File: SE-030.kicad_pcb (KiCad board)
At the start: 4 copper layers, 109.1 x 99.6 mm, 78 parts, among them J1 MacSEPDS, J2 JTAG, SW1 OSCSEL, U1 XC95144XL-TQ100, U10 39SF040, U11 39SF040, U13 74AHCT573, U14 MC68HC000FN20, U15 74AHCT573, U16 74AHCT573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

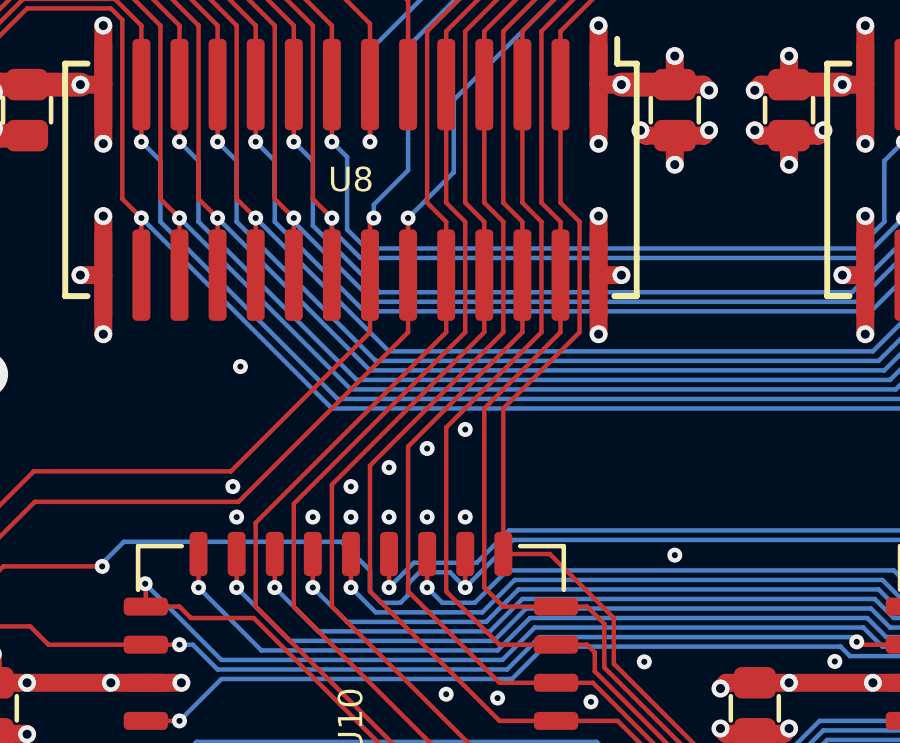
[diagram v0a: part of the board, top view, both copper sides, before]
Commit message: Update SE-030.kicad_pcb
More via stitching
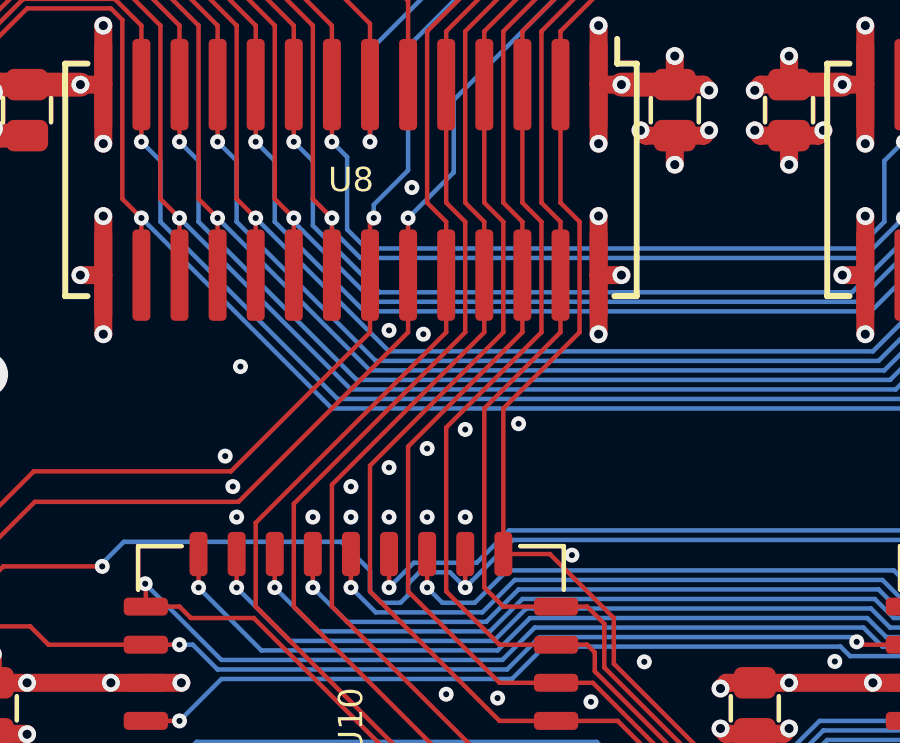
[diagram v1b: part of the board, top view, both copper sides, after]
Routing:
- net GND: vias 428 -> 433

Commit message: Documentation update
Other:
- board text added: "4410A"
- board text removed: "4406A"
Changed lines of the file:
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@@
     (solder_paste_margin -0.025)
     (attr smd)
-    (fp_text reference U14 (at 0 0) (layer F.SilkS)
+    (fp_text reference U14 (at 0 -1.27) (layer F.SilkS)
       (effects (font (size 0.8128 0.8128) (thickness 0.2032)))
     )
@@
     (fp_line (start -12.37 -10.71) (end -12.9 -10.71) (layer F.CrtYd) (width 0.05))
     (fp_line (start -12.9 -10.71) (end -12.9 0) (layer F.CrtYd) (width 0.05))
-    (fp_text user %R (at 0 0) (layer F.Fab)
+    (fp_text user %R (at 0 -1.27) (layer F.Fab)
       (effects (font (size 0.8128 0.8128) (thickness 0.2032)))
     )
@@
     )
   )
-  (gr_text Warp-SE (at 181.356 43.18) (layer F.SilkS)
+  (gr_text Warp-SE (at 181.356 43.815) (layer F.SilkS)
     (effects (font (size 1.524 1.524) (thickness 0.3)))
   )
-  (gr_text "Accelerator for Mac SE" (at 181.356 45.466) (layer F.SilkS)
+  (gr_text "Accelerator for Mac SE" (at 181.356 46.101) (layer F.SilkS)
     (effects (font (size 1.016 1.016) (thickness 0.2032)))
   )
-  (gr_text GW (at 159.258 45.6565) (layer F.SilkS)
+  (gr_text GW (at 159.258 46.2915) (layer F.SilkS)
     (effects (font (size 1.5 1.5) (thickness 0.3)) (justify right))
   )
-  (gr_text 4406A (at 159.258 45.72) (layer F.SilkS)
+  (gr_text 4410A (at 159.258 46.355) (layer F.SilkS)
     (effects (font (size 1.5 1.5) (thickness 0.3)) (justify left))
   )
-  (gr_text "Garrett’s Workshop" (at 161.163 42.926) (layer F.SilkS)
+  (gr_text "Garrett’s Workshop" (at 161.163 43.561) (layer F.SilkS)
     (effects (font (size 1.524 1.524) (thickness 0.225)))
   )
@@
   (segment (start 109.6 108.1) (end 108.9 108.1) (width 0.5) (layer F.Cu) (net 1))
   (via (at 198.882 94.0435) (size 0.5) (drill 0.2) (layers F.Cu B.Cu) (net 1))
-  (via (at 154.94 98.933) (size 0.5) (drill 0.2) (layers F.Cu B.Cu) (net 1))
-  (via (at 156.21 98.933) (size 0.5) (drill 0.2) (layers F.Cu B.Cu) (net 1))
-  (via (at 151.13 98.933) (size 0.5) (drill 0.2) (layers F.Cu B.Cu) (net 1))
-  (via (at 149.86 98.933) (size 0.5) (drill 0.2) (layers F.Cu B.Cu) (net 1))
-  (via (at 148.59 98.933) (size 0.5) (drill 0.2) (layers F.Cu B.Cu) (net 1))
-  (via (at 144.78 98.933) (size 0.5) (drill 0.2) (layers F.Cu B.Cu) (net 1))
-  (via (at 143.51 98.933) (size 0.5) (drill 0.2) (layers F.Cu B.Cu) (net 1))
+  (via (at 154.94 102.6795) (size 0.5) (drill 0.2) (layers F.Cu B.Cu) (net 1))
+  (via (at 156.21 101.4095) (size 0.5) (drill 0.2) (layers F.Cu B.Cu) (net 1))
+  (via (at 151.257 103.759) (size 0.5) (drill 0.2) (layers F.Cu B.Cu) (net 1))
+  (via (at 149.987 103.6955) (size 0.5) (drill 0.2) (layers F.Cu B.Cu) (net 1))
+  (via (at 148.717 102.9335) (size 0.5) (drill 0.2) (layers F.Cu B.Cu) (net 1))
+  (via (at 144.907 102.8065) (size 0.5) (drill 0.2) (layers F.Cu B.Cu) (net 1))
+  (via (at 143.637 102.8065) (size 0.5) (drill 0.2) (layers F.Cu B.Cu) (net 1))
   (via (at 154.94 93.98) (size 0.5) (drill 0.2) (layers F.Cu B.Cu) (net 1))
   (via (at 144.78 93.98) (size 0.5) (drill 0.2) (layers F.Cu B.Cu) (net 1))
@@
   (via (at 114.15 78.35) (size 1) (drill 0.5) (layers F.Cu B.Cu) (net 1))
   (via (at 120.45 96.35) (size 0.5) (drill 0.2) (layers F.Cu B.Cu) (net 1))
-  (via (at 153.67 98.933) (size 0.5) (drill 0.2) (layers F.Cu B.Cu) (net 1))
+  (via (at 153.797 103.759) (size 0.5) (drill 0.2) (layers F.Cu B.Cu) (net 1))
   (via (at 173.228 56.515) (size 0.6) (drill 0.3) (layers F.Cu B.Cu) (net 1))
   (segment (start 173.052 56.691) (end 173.228 56.515) (width 0.6) (layer F.Cu) (net 1))
@@
   (via (at 149.225 81.407) (size 0.5) (drill 0.2) (layers F.Cu B.Cu) (net 1))
   (via (at 147.32 93.98) (size 0.5) (drill 0.2) (layers F.Cu B.Cu) (net 1))
-  (via (at 146.05 98.933) (size 0.5) (drill 0.2) (layers F.Cu B.Cu) (net 1))
-  (via (at 142.24 98.933) (size 0.5) (drill 0.2) (layers F.Cu B.Cu) (net 1))
-  (via (at 157.48 98.933) (size 0.5) (drill 0.2) (layers F.Cu B.Cu) (net 1))
+  (via (at 146.177 102.8065) (size 0.5) (drill 0.2) (layers F.Cu B.Cu) (net 1))
+  (via (at 142.367 102.8065) (size 0.5) (drill 0.2) (layers F.Cu B.Cu) (net 1))
+  (via (at 157.48 100.1395) (size 0.5) (drill 0.2) (layers F.Cu B.Cu) (net 1))
   (via (at 142.113 111.76) (size 0.5) (drill 0.2) (layers F.Cu B.Cu) (net 1))
   (via (at 140.462 120.015) (size 0.5) (drill 0.2) (layers F.Cu B.Cu) (net 1))
@@
   (via (at 151.765 83.693) (size 0.5) (drill 0.2) (layers F.Cu B.Cu) (net 1))
   (via (at 144.145 89.154) (size 0.5) (drill 0.2) (layers F.Cu B.Cu) (net 1))
-  (via (at 147.32 98.933) (size 0.5) (drill 0.2) (layers F.Cu B.Cu) (net 1))
+  (via (at 147.447 102.8065) (size 0.5) (drill 0.2) (layers F.Cu B.Cu) (net 1))
   (via (at 156.21 93.98) (size 0.5) (drill 0.2) (layers F.Cu B.Cu) (net 1))
-  (via (at 152.4 98.933) (size 0.5) (drill 0.2) (layers F.Cu B.Cu) (net 1))
+  (via (at 152.527 103.759) (size 0.5) (drill 0.2) (layers F.Cu B.Cu) (net 1))
   (segment (start 198.82 120.22) (end 199.1 120.5) (width 0.8) (layer F.Cu) (net 1))
   (via (at 199.1 120.5) (size 0.8) (drill 0.4) (layers F.Cu B.Cu) (net 1))
